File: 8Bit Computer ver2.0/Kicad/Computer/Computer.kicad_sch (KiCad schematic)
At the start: 209 parts, among them IC1 MP2338GTL-Z, IC2 MP2338GTL-Z, IC266 SN74LVC1GU04DCKR, IC267 TMUX1309DYYR, IC268 SN74LVC1G14DBVR, IC269 LM555CMX_NOPB, IC270 SN74AHC74DR, IC274 SN74AHC540DWR, IC275 SN74AHC540DWR, IC276 SN74AHC540DWR, IC277 SN74AHC540DWR, IC278 SN74AHC540DWR, IC279 SN74AHC540DWR, IC3 DS1100Z-150+, J1 M20-7910842R, J10 M20-7910842R, J11 M20-7910842R, J12 M20-7910842R, J13 M20-7910842R, J14 M20-7910842R, J15 M20-7910842R, J16 M20-7910842R, J17 M20-7910842R, J18 M20-8890845, J19 M20-8890845, J2 M20-7910842R, J20 M20-8890845, J21 M20-8890845, J22 M20-8890845, J23 M20-8890845, J24 M20-8890845, J25 M20-8890845, J26 M20-8890845, J27 M20-8890845, J28 M20-8890845, J29 M20-8890845, J3 M20-7910842R, J30 M20-8890845, J31 M20-8890845, J32 M20-8890845, J33 M20-8890845, J34 M20-8890845, J38 M20-7910842R, J39 M20-7910842R, J4 M20-7910842R, J40 M20-7911042R, J41 M20-7911042R, J5 M20-7910842R, J6 M20-7910842R, J7 M20-7910842R, J8 M20-7910842R, J9 M20-7910842R, Y1 8MHz

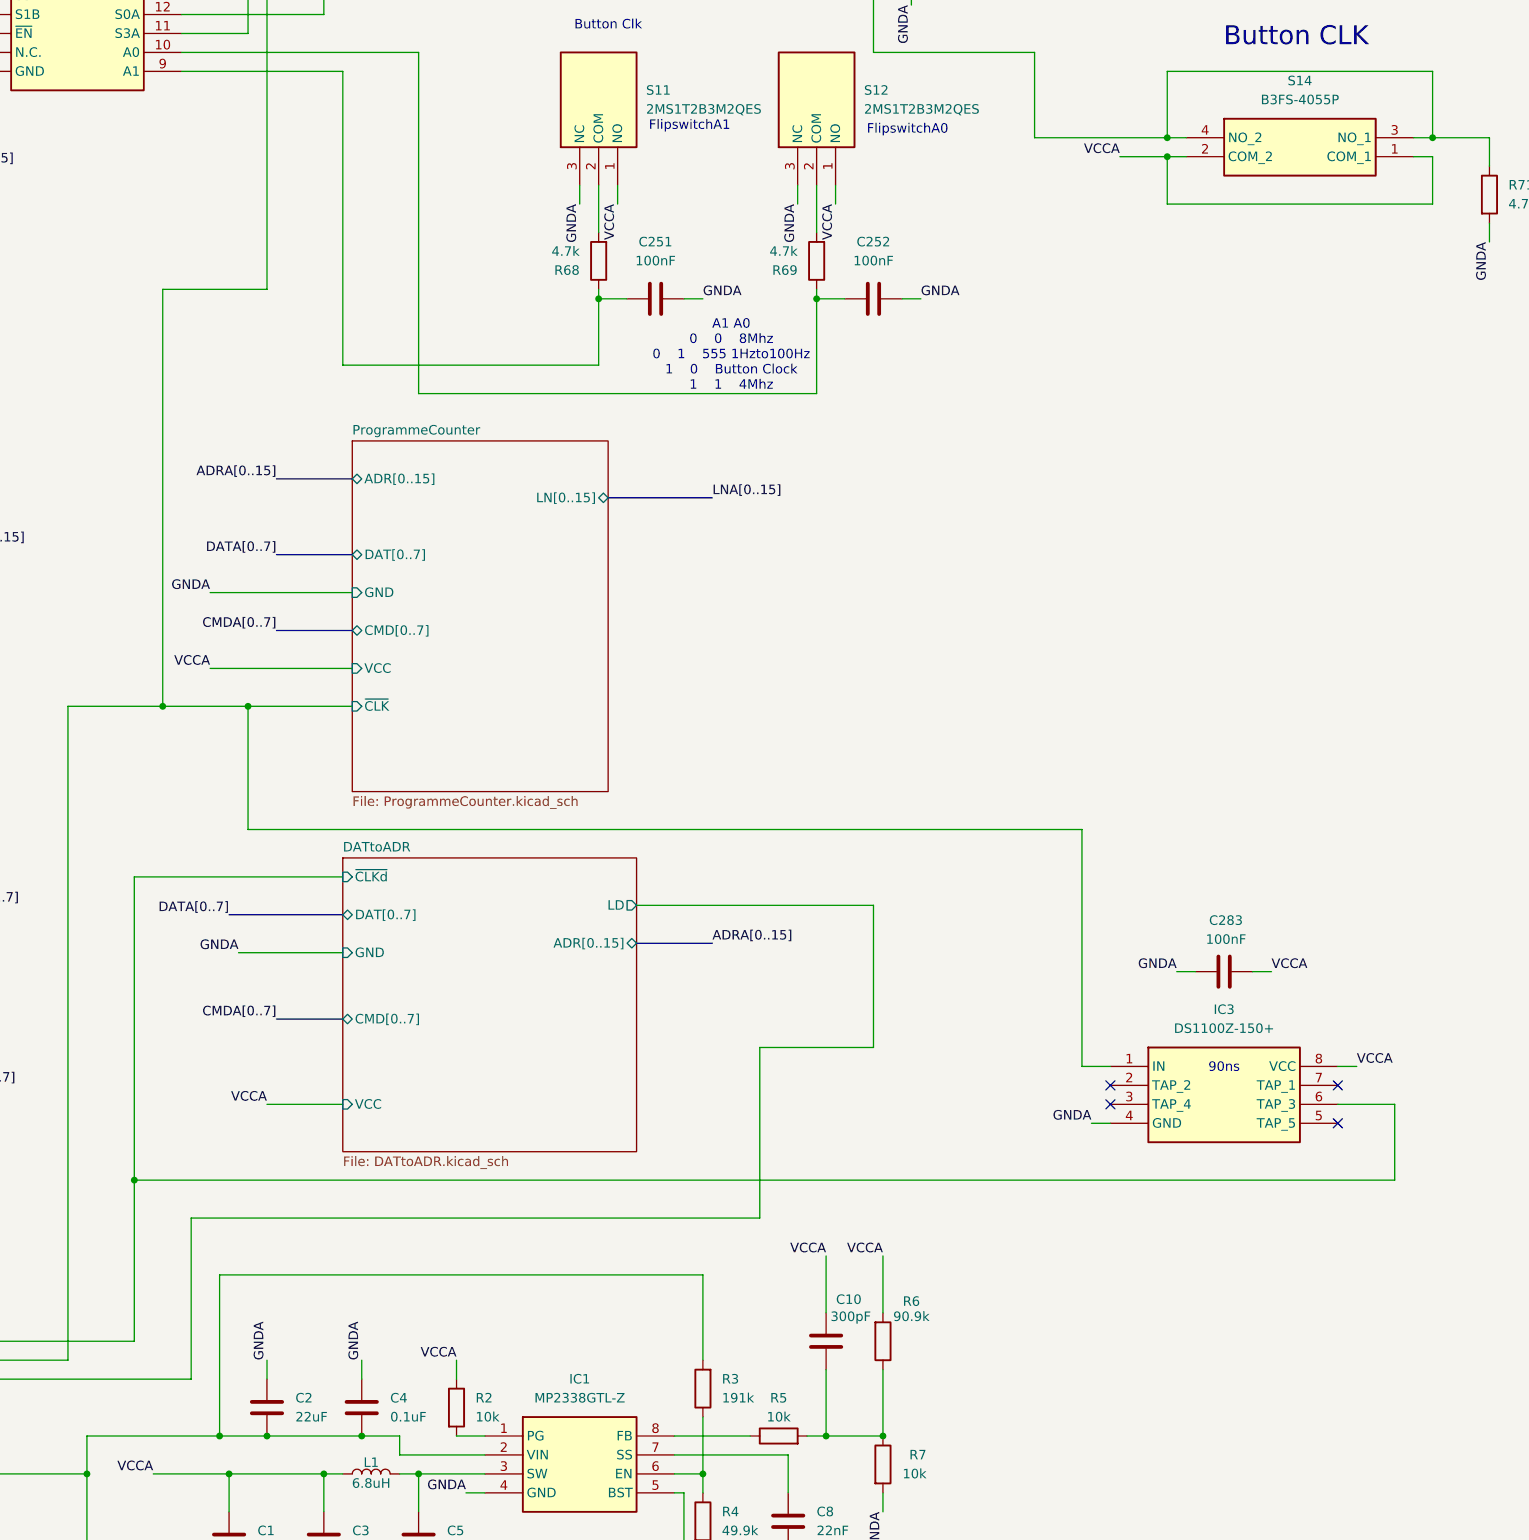
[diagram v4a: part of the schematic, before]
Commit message: Kicad
fixed some design errors(dat dis DistShiftreg, wrong cmd pins)
added description to every CMD for better debug, use CTRL+f and use option "Whole words only" to search e.g. inc
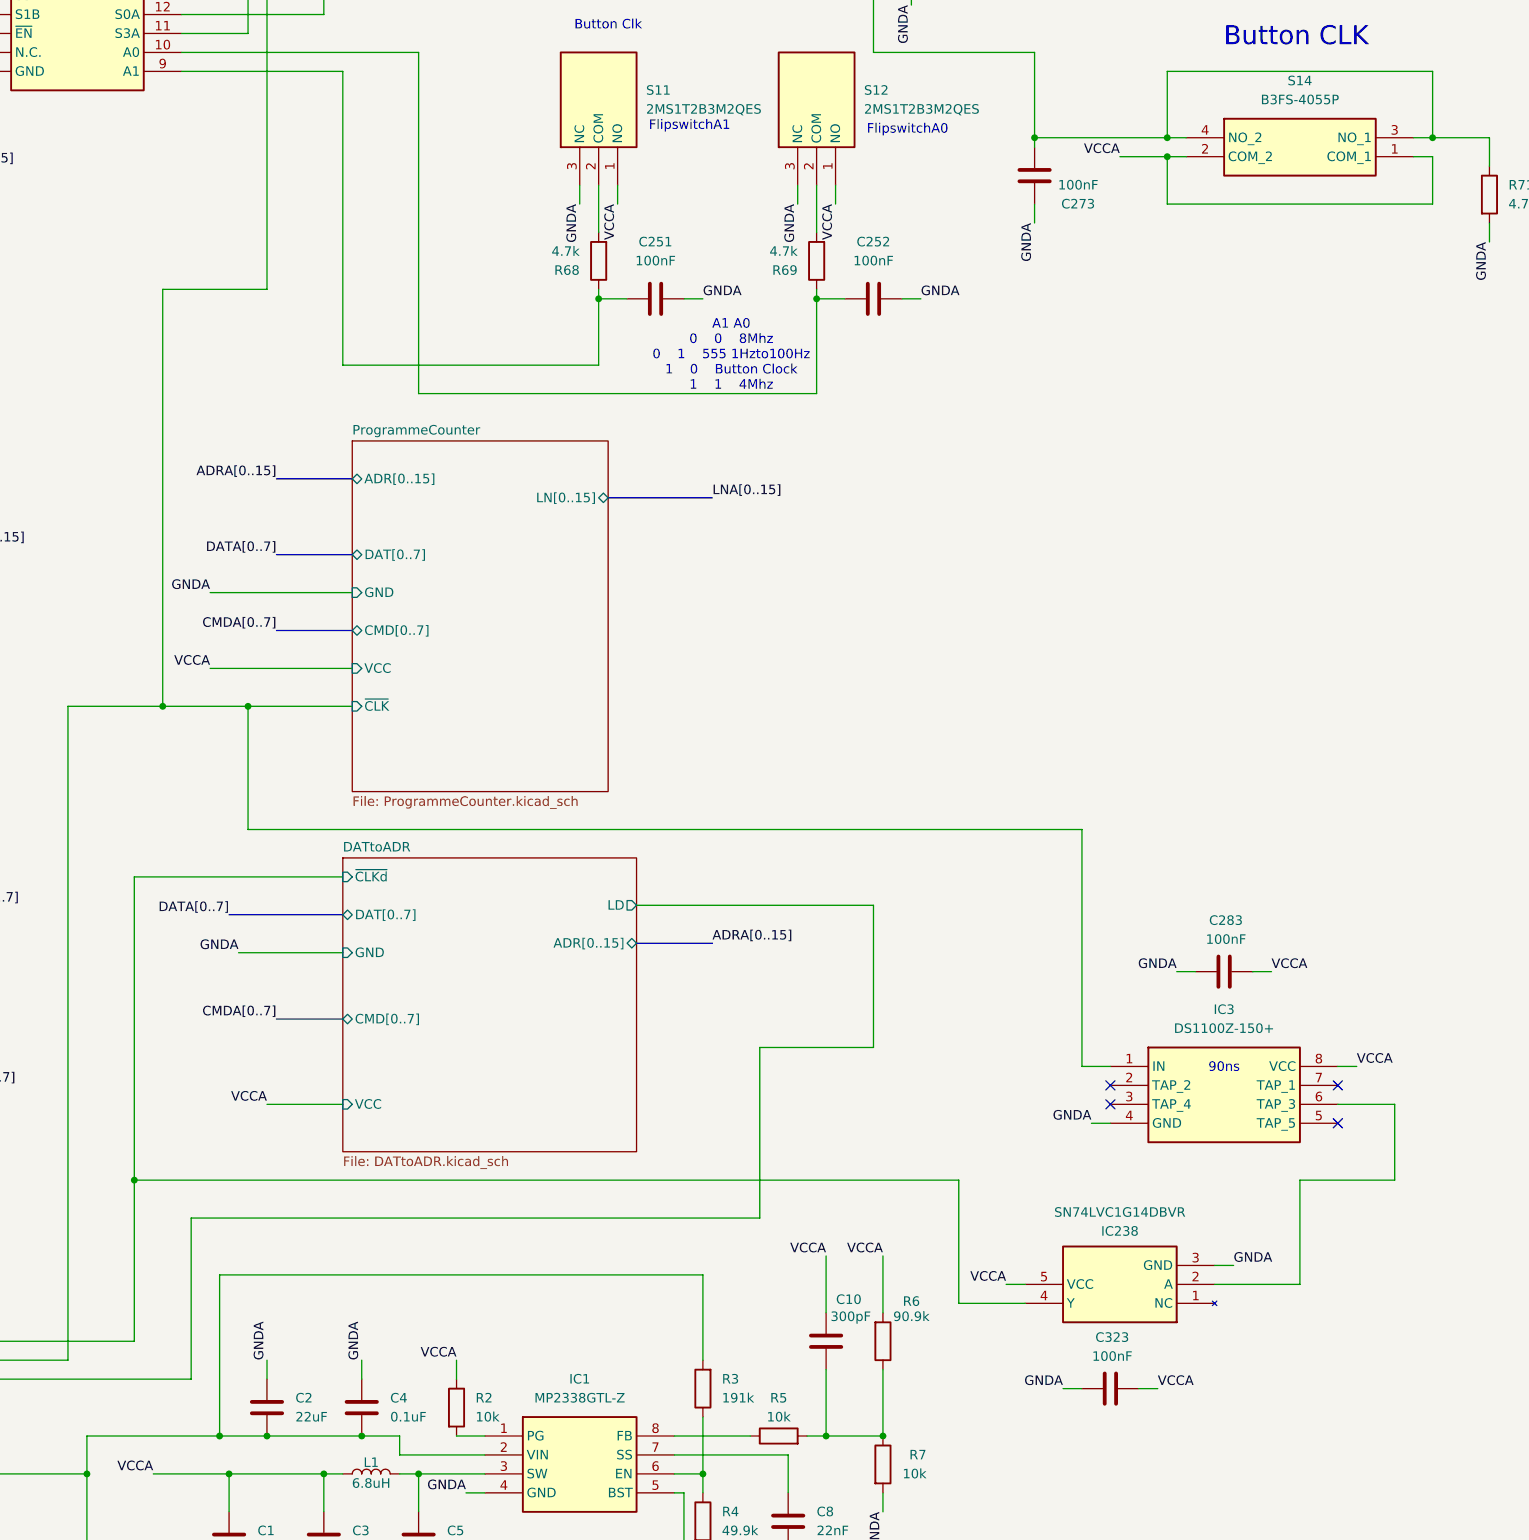
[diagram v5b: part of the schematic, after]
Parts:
- added C273, C323: 100nF, Capacitor_SMD:C_1206_3216Metric_Pad1.33x1.80mm_HandSolder, symbol Device:C
- added IC238: SN74LVC1G14DBVR, Samacsys:SOT95P280X145-5N, symbol Samacsys:SN74LVC1G14DBVR
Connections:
- net DATtoADR/~{CLKd}: now also IC238.4 (Y); no longer IC3.6 (TAP_3)
- net GNDA: now also C273.1, C323.2, IC238.3 (GND)
- net VCCA: now also C323.1, IC238.5 (VCC)
- net at IC267.14 (S1A), R71.1, S14.3 (NO_1)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: now also C273.2
- new net: IC238.2 (A), IC3.6 (TAP_3)

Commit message: Fixed some Design bugs
added some pdfs
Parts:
- Y1: value 8MHz -> 4MHz
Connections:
- net DATtoADR/~{CLKd} renamed ~{CLKMd}
- net ProgrammeCounter/~{CLK} renamed CLKM
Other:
- note added: "555-Timer Clock"
- note added: "Dlatch for 4Mhz to 2Mhz"
- note added: "Pierce Oscillator"
- note removed: "Button Clk"
- note removed: "Dlatch for 8Mhz to 4Mhz"
- moved on the sheet: C243, C244, C245, C246, C247, C248, C249, C250, C251, C252, C253, C254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

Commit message: changed page numbers, compressed ROOT file from A1 to A4
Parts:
- removed C1, C2, C3, C6, C7, C9: 22uF, Capacitor_SMD:C_1206_3216Metric_Pad1.33x1.80mm_HandSolder, symbol Device:C
- removed C10, C14: 300pF, Capacitor_SMD:C_1206_3216Metric_Pad1.33x1.80mm_HandSolder, symbol Device:C
- removed C11, C12, C4, C5: 0.1uF, Capacitor_SMD:C_1206_3216Metric_Pad1.33x1.80mm_HandSolder, symbol Device:C
- removed C13, C8: 22nF, Capacitor_SMD:C_1206_3216Metric_Pad1.33x1.80mm_HandSolder, symbol Device:C
- removed C243, C245: 27pF, Capacitor_SMD:C_1206_3216Metric_Pad1.33x1.80mm_HandSolder, symbol Device:C
- removed C244, C246, C247, C248, C251, C252, C253, C254, C273, C283, C323: 100nF, Capacitor_SMD:C_1206_3216Metric_Pad1.33x1.80mm_HandSolder, symbol Device:C
- removed C249: 10nF, Capacitor_SMD:C_1206_3216Metric_Pad1.33x1.80mm_HandSolder, symbol Device:C
- removed C250: 4.7uF, Capacitor_SMD:C_1206_3216Metric_Pad1.33x1.80mm_HandSolder, symbol Device:C
- removed IC1, IC2: MP2338GTL-Z, Samacsys:MP2338GTLZ, symbol Samacsys:MP2338GTL-Z
- removed IC238, IC268: SN74LVC1G14DBVR, Samacsys:SOT95P280X145-5N, symbol Samacsys:SN74LVC1G14DBVR
- removed IC266: SN74LVC1GU04DCKR, Samacsys:SOT65P210X110-5N, symbol Samacsys:SN74LVC1GU04DCKR
- removed IC267: TMUX1309DYYR, Samacsys:SOP50P326X110-16N, symbol Samacsys:TMUX1309DYYR
- removed IC269: LM555CMX_NOPB, Samacsys:SOIC127P600X175-8N, symbol Samacsys:LM555CMX_NOPB
- removed IC270: SN74AHC74DR, Samacsys:SOIC127P600X175-14N, symbol Samacsys:SN74AHC74DR
- removed IC274, IC275, IC276, IC277, IC278, IC279: SN74AHC540DWR, Samacsys:SOIC127P1030X265-20N, symbol Samacsys:SN74AHC540DWR
- removed IC3: DS1100Z-150+, Samacsys:SOIC127P600X175-8N, symbol Samacsys:DS1100Z-150+
- removed J1, J10, J11, J12, J13, J14, J2, J3, J4, J5, J6, J7, J8, J9: M20-7910842R, Samacsys:M207910842R, symbol Samacsys:M20-7910842R
- removed J18, J19, J20, J21, J22, J23, J24, J25, J26, J27, J28, J29, J30, J31: M20-8890845, Samacsys:M208890845, symbol Samacsys:M20-8890845
- removed L1, L2: 6.8uH, Samacsys:INDPM108100X400N, symbol Device:L
- removed LED100, LED101, LED102, LED103, LED104, LED97, LED98, LED99: LTST-C170KRKT, Samacsys:LEDC2012X120N, symbol Samacsys:LTST-C170KRKT
- removed LED57, LED58, LED59, LED60, LED61, LED62, LED63, LED64, LED65, LED66, LED67, LED68, LED69, LED70, LED71, LED72: LTST-C171KSKT, Samacsys:LTSTC171KSKT, symbol Samacsys:LTST-C171KSKT
- removed LED73, LED74, LED75, LED76, LED77, LED78, LED79, LED80, LED81, LED82, LED83, LED84, LED85, LED86, LED87, LED89: LTST-C170KGKT, Samacsys:LEDC2012X110N, symbol Samacsys:LTST-C170KGKT
- removed LED88, LED90, LED91, LED92, LED93, LED94, LED95, LED96: LTST-C170KFKT, Samacsys:LEDC2012X120N, symbol Samacsys:LTST-C170KFKT
- removed R10, R4: 49.9k, Resistor_SMD:R_1206_3216Metric_Pad1.30x1.75mm_HandSolder, symbol Device:R
- removed R11, R13, R2, R5, R7, R8: 10k, Resistor_SMD:R_1206_3216Metric_Pad1.30x1.75mm_HandSolder, symbol Device:R
- removed R112, R113, R114, R115, R116, R117, R118, R119, R120, R121, R122, R123, R124, R125, R126, R127, R128, R129, R130, R131, R132, R133, R134, R135, R136, R137, R138, R139, R140, R141, R142, R143, R144, R145, R146, R147, R148, R149, R150, R151, R152, R153, R154, R155, R156, R157, R158, R159: 390, Resistor_SMD:R_1206_3216Metric_Pad1.30x1.75mm_HandSolder, symbol Device:R
- removed R12, R6: 90.9k, Resistor_SMD:R_1206_3216Metric_Pad1.30x1.75mm_HandSolder, symbol Device:R
- removed R3, R9: 191k, Resistor_SMD:R_1206_3216Metric_Pad1.30x1.75mm_HandSolder, symbol Device:R
- removed R62, R68, R69, R70, R71: 4.7k, Resistor_SMD:R_1206_3216Metric_Pad1.30x1.75mm_HandSolder, symbol Device:R
- removed R63, R66: 1M, Resistor_SMD:R_1206_3216Metric_Pad1.30x1.75mm_HandSolder, symbol Device:R
- removed R64: 330, Resistor_SMD:R_1206_3216Metric_Pad1.30x1.75mm_HandSolder, symbol Device:R
- removed R65: 100, Resistor_SMD:R_1206_3216Metric_Pad1.30x1.75mm_HandSolder, symbol Device:R
- removed R67: 1500, Resistor_SMD:R_1206_3216Metric_Pad1.30x1.75mm_HandSolder, symbol Device:R
- removed S11, S12, S13: 2MS1T2B3M2QES, Samacsys:2MS1T2B3M2QES, symbol Samacsys:2MS1T2B3M2QES
- removed S14: B3FS-4055P, Samacsys:B3FS4055P, symbol Samacsys:B3FS-4055P
- removed U1: ~, Samacsys:USB_C_PD_Triggerboard, symbol Samacsys:USB_C_PD_Triggerboard
- removed VR1: M61P104KT20T607, Samacsys:M61P104KT20T607, symbol Samacsys:M61P104KT20T607
- removed Y1: 4MHz, Crystal:Crystal_SMD_HC49-SD_HandSoldering, symbol Device:Crystal
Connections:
- net DAT_{dis}: now reaches D27.1 (K), J17.8
- no-connect marks 21 -> 4
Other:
- removed sheet DATtoADR
- removed sheet FlashMemory
- removed sheet ProgrammeCounter
- removed sheet RAM
- added sheet ADR_Bus_LEDs_ALU (ADR_Bus_LEDs_ALU.kicad_sch)
- added sheet ALU_Control_Module (ALU_Control_Module.kicad_sch)
- added sheet ALU_Memory_Module (ALU_Memory_Module.kicad_sch)
- added sheet CMDDAT_Bus_LEDs_ALU (CMDDAT_Bus_LEDs_ALU.kicad_sch)
- added sheet Control_Module (Control_Module.kicad_sch)
- added sheet LN_Bus_LEDs_ALU (LN_Bus_LEDs_ALU.kicad_sch)
- added sheet Memory_Module (Memory_Module.kicad_sch)
- note removed: "555-Timer Clock"
- note removed: "90ns"
- note removed: "A1 A0 0 0 8Mhz 0 1 555 1Hzto100Hz 1 0 Button Clock 1 1 4Mhz"
- note removed: "Button CLK"
- note removed: "Dlatch for 4Mhz to 2Mhz"
- note removed: "EN"
- note removed: "FlipswitchA0"
- note removed: "FlipswitchA1"
- note removed: "Pierce Oscillator"
- moved on the sheet: C322, D27, J15, J16, J17, J32, J33, J34, J38, J39, J40, J41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

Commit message: changed page numbers, every schematic is now A4
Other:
- title: (none) -> ${SHEETNAME}
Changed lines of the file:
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@@
 	(generator_version "9.0")
 	(paper "A4")
+	(title_block
+		(title "${SHEETNAME}")
+		(date "2026-03-21")
+		(rev "2.7")
+	)
 	(junction
 		(at 144.78 118.11)
@@
 			(project "Computer"
 				(path "/1196a00e-6878-4d6d-82b7-9e052dfe7c14"
-					(page "22")
+					(page "44")
 				)
 			)
@@
 			(project "Computer"
 				(path "/1196a00e-6878-4d6d-82b7-9e052dfe7c14"
-					(page "29")
+					(page "30")
 				)
 			)
@@
 			(project "Computer"
 				(path "/1196a00e-6878-4d6d-82b7-9e052dfe7c14"
-					(page "35")
+					(page "36")
 				)
 			)
@@
 			(project "Computer"
 				(path "/1196a00e-6878-4d6d-82b7-9e052dfe7c14"
-					(page "36")
+					(page "37")
 				)
 			)
@@
 			(project "Computer"
 				(path "/1196a00e-6878-4d6d-82b7-9e052dfe7c14"
-					(page "37")
+					(page "38")
 				)
 			)
@@
 			(project "Computer"
 				(path "/1196a00e-6878-4d6d-82b7-9e052dfe7c14"
-					(page "99")
+					(page "39")
 				)
 			)
@@
 			(project "Computer"
 				(path "/1196a00e-6878-4d6d-82b7-9e052dfe7c14"
-					(page "33")
+					(page "34")
 				)
 			)
@@
 			(project "Computer"
 				(path "/1196a00e-6878-4d6d-82b7-9e052dfe7c14"
-					(page "34")
+					(page "35")
 				)
 			)
